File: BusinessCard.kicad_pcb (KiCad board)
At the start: 4 copper layers, 88.9 x 50.8 mm, 94 parts, among them J1 USB_OTG, J2 RNG, J3 X, J4 Trigger, J5 Y, Q1 2N3904, Q2 2N3904, U1 TLE2426, U10 SN74LVC2G14DBVR, U11 SN74LVC2G14DBVR, U12 74HC74, U13 74HC74, U14 74HC74, U15 74HC74, U16 LTC6241, U2 TLV271, U3 TLV3201, U4 SN74LVC1G175, U5 LTC6241, U6 SN74LVC1G66, U7 SN74LVC1G66, U8 SN74LVC1G66, U9 SN74LVC1G66

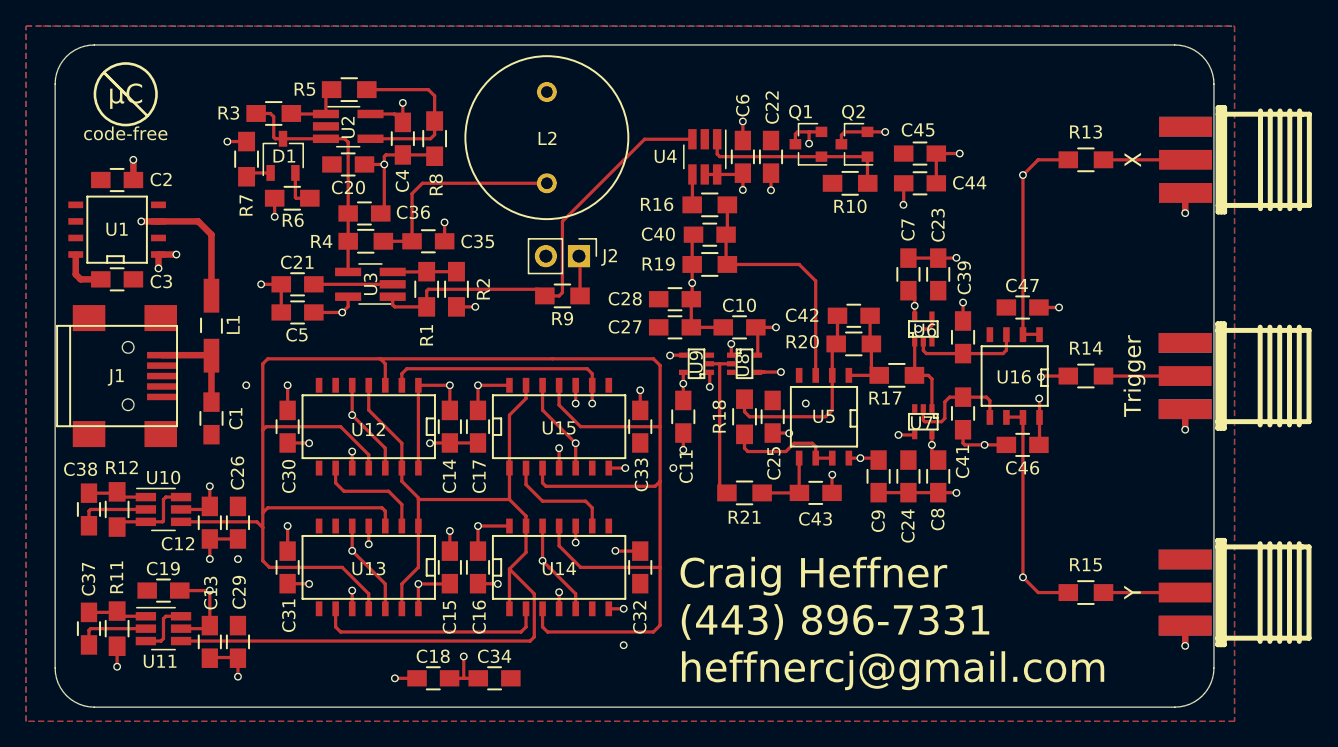
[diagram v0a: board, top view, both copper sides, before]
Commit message: Fixed pin numbering on Q1, Q2. Changed op amp part numbers.
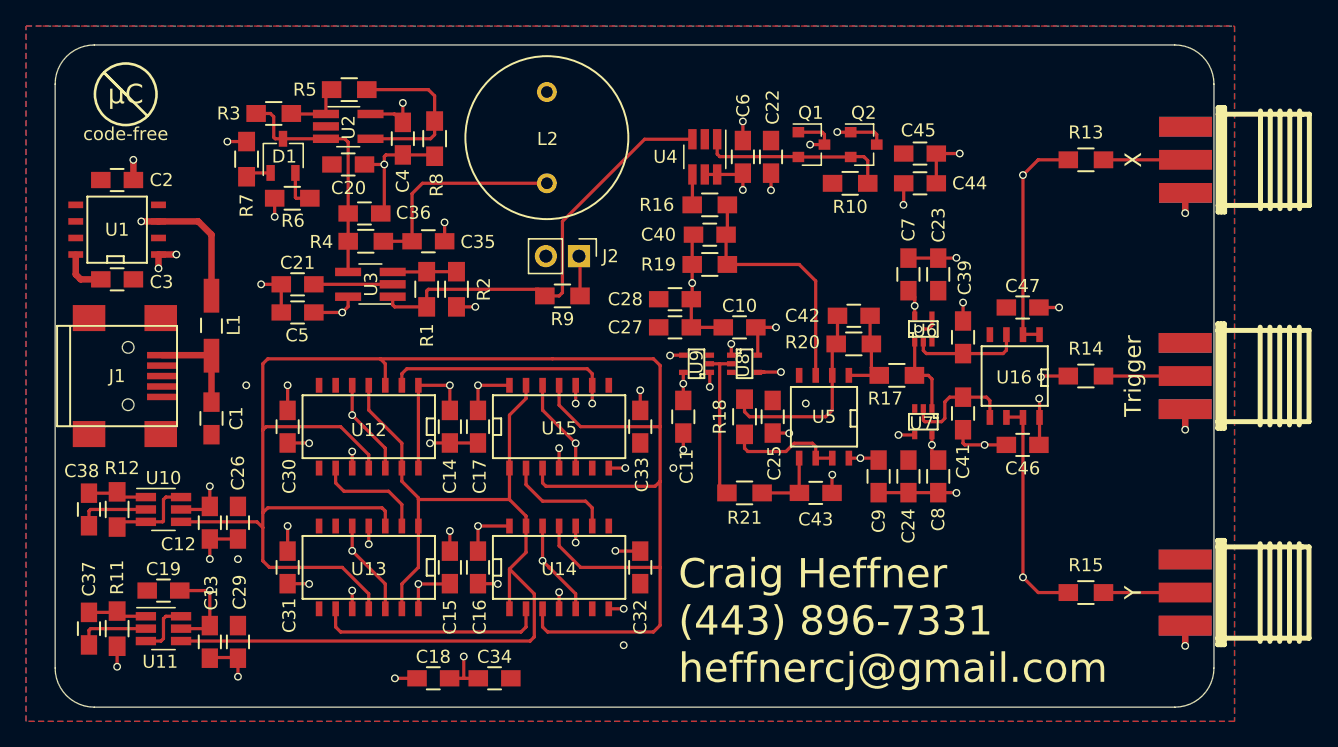
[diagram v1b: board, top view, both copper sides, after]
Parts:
- Q1, Q2: value 2N3904 -> MMBT3904
- U16, U5: value LTC6241 -> TLV272
- moved Q2 0.71 mm to (167.1, 78.9), turned to 0 degrees
- moved Q1 0.23 mm to (163.1, 78.9), turned to 0 degrees
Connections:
- Q1 pad 1: Net-(Q1-Pad1) -> CLOCK_CYCLE_0
- Q1 pad 2: CLOCK_CYCLE_0 -> Net-(Q1-Pad2)
- Q2 pad 1: Net-(Q1-Pad1) -> CLOCK_CYCLE_2
- Q2 pad 2: CLOCK_CYCLE_2 -> Net-(Q1-Pad2)
- R10 pad 1: Net-(Q1-Pad1) -> Net-(Q1-Pad2)
- U4 pad 1: Net-(Q1-Pad1) -> Net-(Q1-Pad2)
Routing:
- net Net-(Q1-Pad1): track 14.8 -> 0.00 mm
- net Net-(Q1-Pad2): track 0.00 -> 14.7 mm
- net CLOCK_CYCLE_2: track 69.1 -> 65.1 mm
